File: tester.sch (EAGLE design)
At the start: 73 parts, among them IC1 ATmega8/88/168, K1 NA 05W K, M1 SP6000C-180, P1 250, P2 10k lin, Q1 BC847CSMD, Q2 BC847CSMD, Q3 BC807-40SMD, Q4 8,000 MHz, Q5 BC847CSMD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

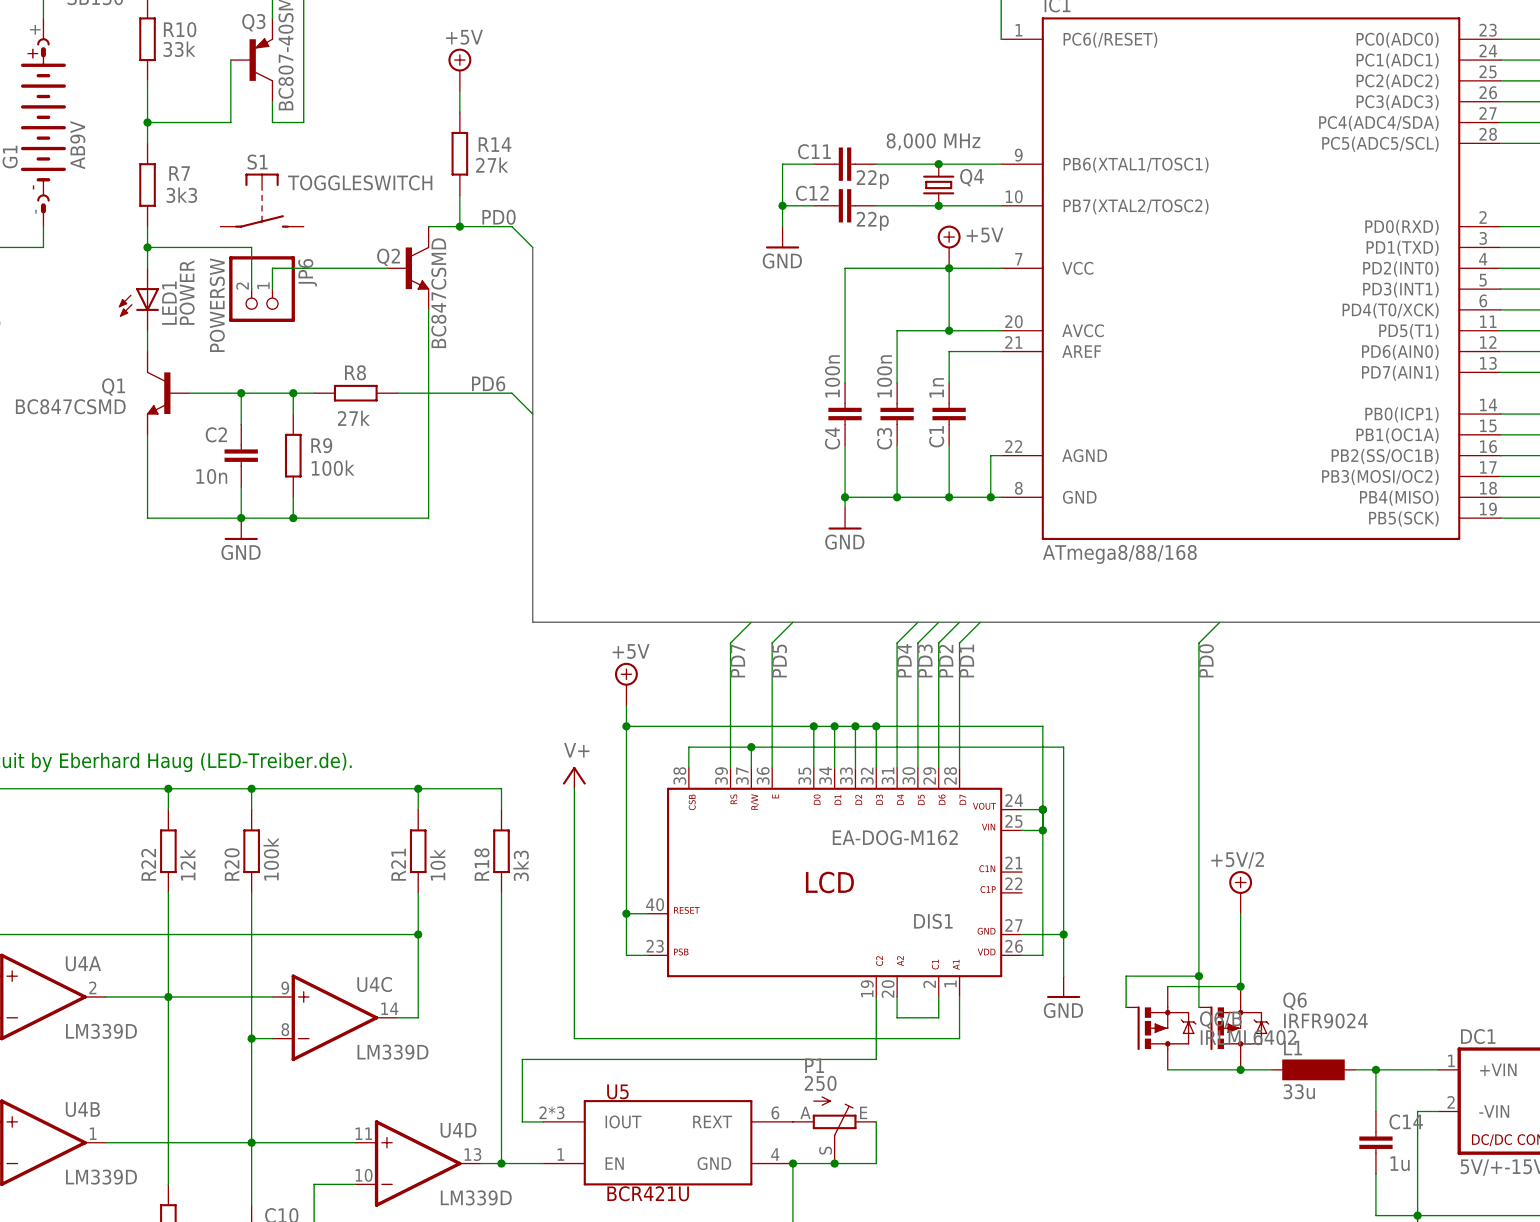
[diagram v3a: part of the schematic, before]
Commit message: change q6, s1
remove q6 option for irfr9024
tactile switch s1 instead of pin header
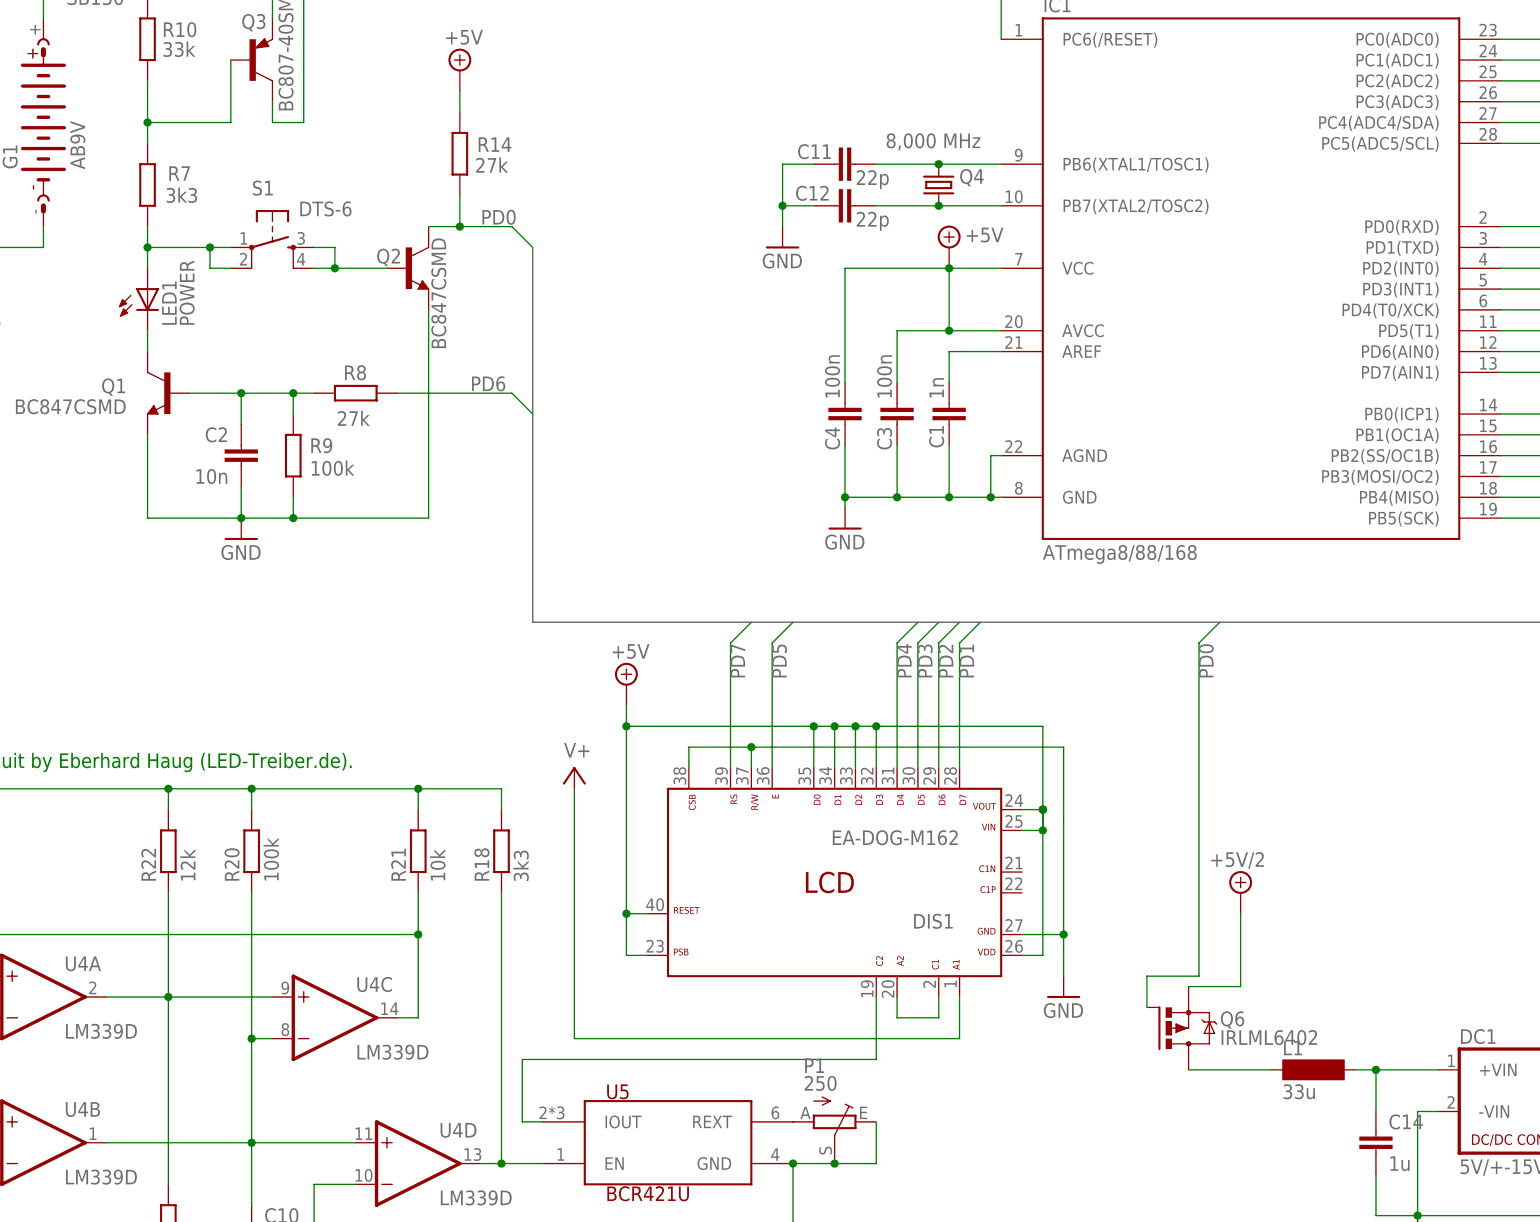
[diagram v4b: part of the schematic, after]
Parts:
- removed JP6: POWERSW, pinhead:PINHD-1X2
- removed Q6/B: IRLML6402, mosfet:IRLML6402
- D2: device markus:SCHOTTKY-DIODE_3-10 -> markus:SCHOTTKY-DIODE_RAD3-5-A
- Q6: value IRFR9024 -> IRLML6402; device transistor-power:IRFR5305 -> mosfet:IRLML6402
- S1: value TOGGLESWITCH -> DTS-6; device external:TOGGLESWITCH -> switch-tact:DTS-6
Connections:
- net +5V/2: no longer Q6/B.S
- net N$21: now also S1.1, S1.2; no longer JP6.2
- net N$24: no longer Q6/B.D
- net N$3: now also S1.3, S1.4; no longer JP6.1
- net PD0: no longer Q6/B.G
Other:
- moved on the sheet: Q6

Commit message: bigger pads for L1
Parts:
- L1: device inductor-neosid:SM-NE29 -> inductor-neosid:SM-NE29BIGGERPAD
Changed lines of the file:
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@@
 <part name="GND8" library="supply1" deviceset="GND" device=""/>
 <part name="X1" library="con-lumberg" deviceset="NEB21R" device=""/>
-<part name="L1" library="inductor-neosid" deviceset="SM-NE29" device="" value="33u"/>
+<part name="L1" library="inductor-neosid" deviceset="SM-NE29" device="BIGGERPAD" value="33u"/>
 <part name="SUPPLY3" library="supply2" deviceset="+5V/2" device=""/>
 <part name="GND3" library="supply1" deviceset="GND" device=""/>

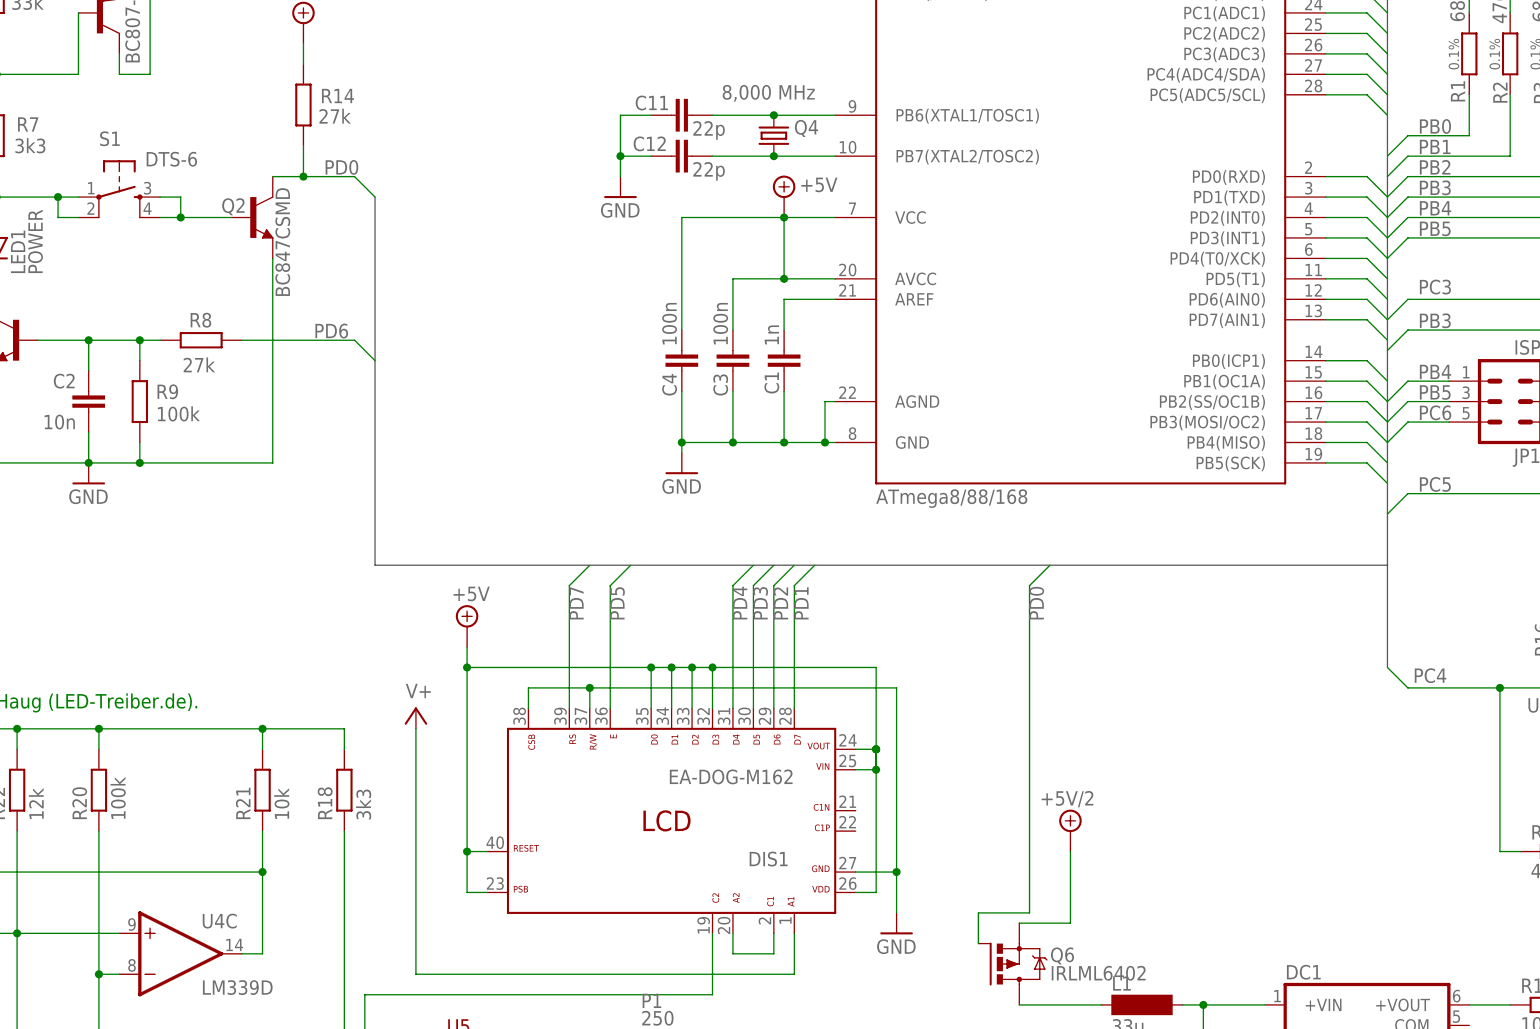
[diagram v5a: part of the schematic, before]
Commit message: added rotary encoder
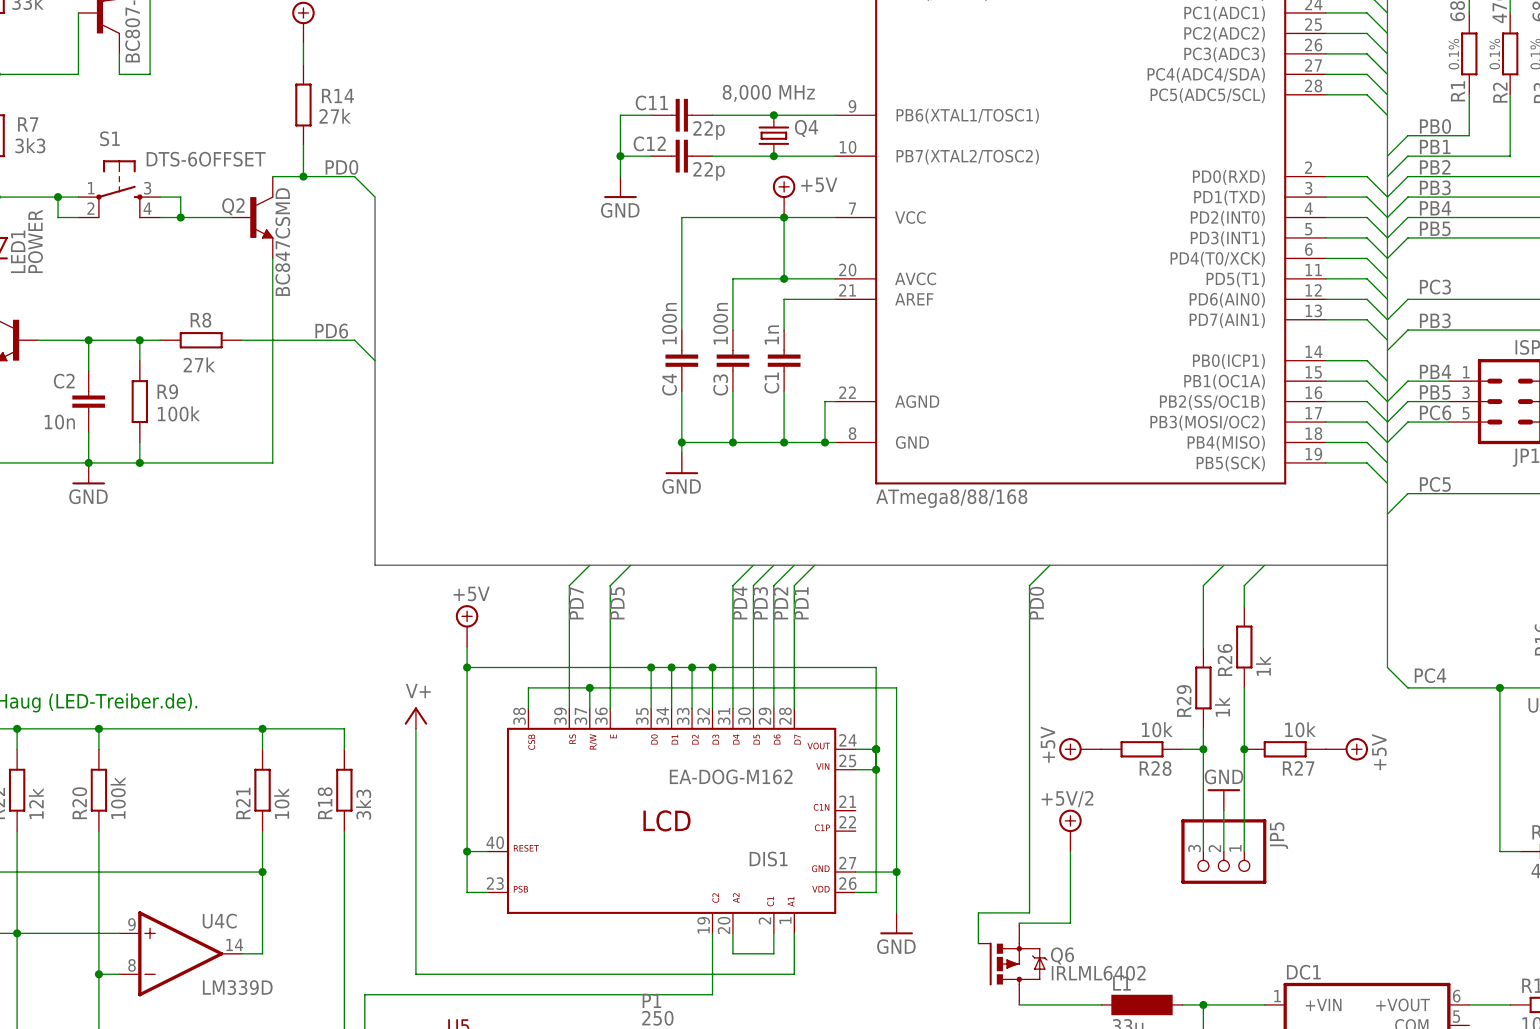
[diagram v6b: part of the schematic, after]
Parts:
- added JP5: (no value), pinhead:PINHD-1X3
- added R26, R29: 1k, resistor:R-EU_R0805
- added R27, R28: 10k, resistor:R-EU_R0805
- S1: value DTS-6 -> DTS-6OFFSET; device switch-tact:DTS-6 -> switch-tact:DTS-6OFFSET
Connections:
- new net N$14: JP5.3, R28.1, R29.1
- new net N$19: JP5.1, R26.1, R27.2
- net +5V: now also R27.1, R28.2
- net GND: now also JP5.2
- net PD2: now also R29.2
- net PD3: now also R26.2
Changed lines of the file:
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@@
 <part name="GND12" library="supply1" deviceset="GND" device=""/>
 <part name="Q6" library="mosfet" deviceset="IRLML6402" device=""/>
-<part name="S1" library="switch-tact" deviceset="DTS-6" device=""/>
+<part name="S1" library="switch-tact" deviceset="DTS-6" device="OFFSET" value="DTS-6OFFSET"/>
+<part name="JP5" library="pinhead" deviceset="PINHD-1X3" device=""/>
+<part name="GND13" library="supply1" deviceset="GND" device=""/>
+<part name="R29" library="resistor" deviceset="R-EU_" device="R0805" value="1k"/>
+<part name="R26" library="resistor" deviceset="R-EU_" device="R0805" value="1k"/>
+<part name="R27" library="resistor" deviceset="R-EU_" device="R0805" value="10k"/>
+<part name="R28" library="resistor" deviceset="R-EU_" device="R0805" value="10k"/>
+<part name="P+6" library="supply2" deviceset="+5V" device=""/>
+<part name="P+9" library="supply2" deviceset="+5V" device=""/>
 </parts>
 <sheets>
@@
 <instance part="Q6" gate="G$1" x="190.5" y="80.01"/>
 <instance part="S1" gate="G$1" x="81.28" y="175.26" rot="R270"/>
+<instance part="JP5" gate="A" x="218.44" y="91.44" rot="R270"/>
+<instance part="GND13" gate="1" x="218.44" y="101.6" rot="R180"/>
+<instance part="R29" gate="G$1" x="215.9" y="114.3" rot="R90"/>
+<instance part="R26" gate="G$1" x="220.98" y="119.38" rot="R90"/>
+<instance part="R27" gate="G$1" x="226.06" y="106.68" rot="R180"/>
+<instance part="R28" gate="G$1" x="208.28" y="106.68" rot="R180"/>
+<instance part="P+6" gate="+5V" x="200.66" y="106.68" rot="R90"/>
+<instance part="P+9" gate="+5V" x="233.68" y="106.68" rot="R270"/>
 </instances>
 <busses>
@@
 <wire x1="274.32" y1="87.63" x2="274.32" y2="88.9" width="0.1524" layer="91"/>
 </segment>
+<segment>
+<pinref part="JP5" gate="A" pin="2"/>
+<pinref part="GND13" gate="1" pin="GND"/>
+<wire x1="218.44" y1="99.06" x2="218.44" y2="93.98" width="0.1524" layer="91"/>
+</segment>
 </net>
 <net name="N$5" class="0">
@@
 <wire x1="162.56" y1="111.76" x2="162.56" y2="127" width="0.1524" layer="91"/>
 </segment>
+<segment>
+<wire x1="218.44" y1="129.54" x2="215.9" y2="127" width="0.1524" layer="91"/>
+<pinref part="R29" gate="G$1" pin="2"/>
+<wire x1="215.9" y1="127" x2="215.9" y2="119.38" width="0.1524" layer="91"/>
+</segment>
 </net>
 <net name="PD3" class="0">
@@
 <pinref part="DIS1" gate="G$1" pin="30"/>
 <wire x1="160.02" y1="111.76" x2="160.02" y2="127" width="0.1524" layer="91"/>
+</segment>
+<segment>
+<wire x1="223.52" y1="129.54" x2="220.98" y2="127" width="0.1524" layer="91"/>
+<pinref part="R26" gate="G$1" pin="2"/>
+<wire x1="220.98" y1="127" x2="220.98" y2="124.46" width="0.1524" layer="91"/>
 </segment>
 </net>
@@
 <junction x="124.46" y="93.98"/>
 </segment>
+<segment>
+<pinref part="R28" gate="G$1" pin="2"/>
+<pinref part="P+6" gate="+5V" pin="+5V"/>
+</segment>
+<segment>
+<pinref part="R27" gate="G$1" pin="1"/>
+<pinref part="P+9" gate="+5V" pin="+5V"/>
+</segment>
 </net>
 <net name="PC0" class="0">
@@
 </segment>
 </net>
+<net name="N$14" class="0">
+<segment>
+<pinref part="R28" gate="G$1" pin="1"/>
+<wire x1="213.36" y1="106.68" x2="215.9" y2="106.68" width="0.1524" layer="91"/>
+<pinref part="R29" gate="G$1" pin="1"/>
+<wire x1="215.9" y1="106.68" x2="215.9" y2="109.22" width="0.1524" layer="91"/>
+<pinref part="JP5" gate="A" pin="3"/>
+<wire x1="215.9" y1="106.68" x2="215.9" y2="93.98" width="0.1524" layer="91"/>
+<junction x="215.9" y="106.68"/>
+</segment>
+</net>
+<net name="N$19" class="0">
+<segment>
+<pinref part="R26" gate="G$1" pin="1"/>
+<pinref part="R27" gate="G$1" pin="2"/>
+<wire x1="220.98" y1="114.3" x2="220.98" y2="106.68" width="0.1524" layer="91"/>
+<pinref part="JP5" gate="A" pin="1"/>
+<wire x1="220.98" y1="106.68" x2="220.98" y2="93.98" width="0.1524" layer="91"/>
+<junction x="220.98" y="106.68"/>
+</segment>
+</net>

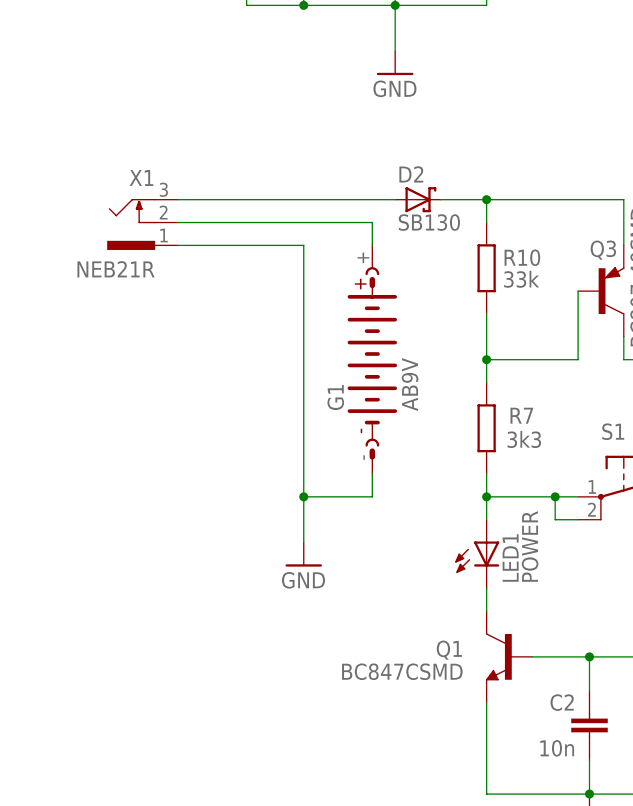
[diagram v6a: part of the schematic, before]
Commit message: normal polarity for neb21, gnd is outside
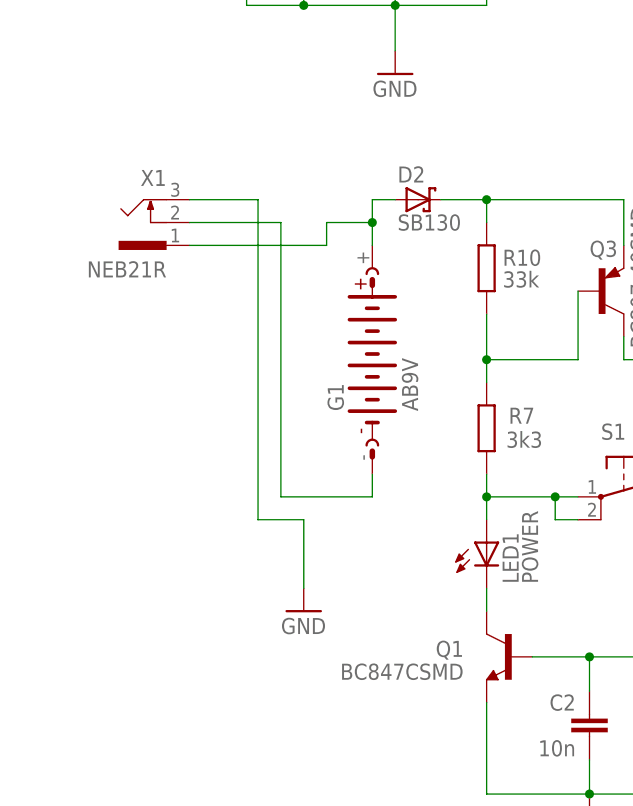
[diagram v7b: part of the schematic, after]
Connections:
- removed net N$11: D2.A, X1.3
- removed net N$9 (its old number): G1.+, X1.2
- new net N$23: D2.A, G1.+, X1.1
- new net N$5: G1.-, X1.2
- net GND: now also X1.3; no longer G1.-, X1.1
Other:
- moved on the sheet: X1
